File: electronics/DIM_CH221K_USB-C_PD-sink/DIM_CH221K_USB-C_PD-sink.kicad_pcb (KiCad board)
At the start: 2 copper layers, 17.3 x 18.5 mm, 15 parts, among them J1 USB-C_PD, J2 Conn_01x04, J3 Conn_01x04, U1 CH221K

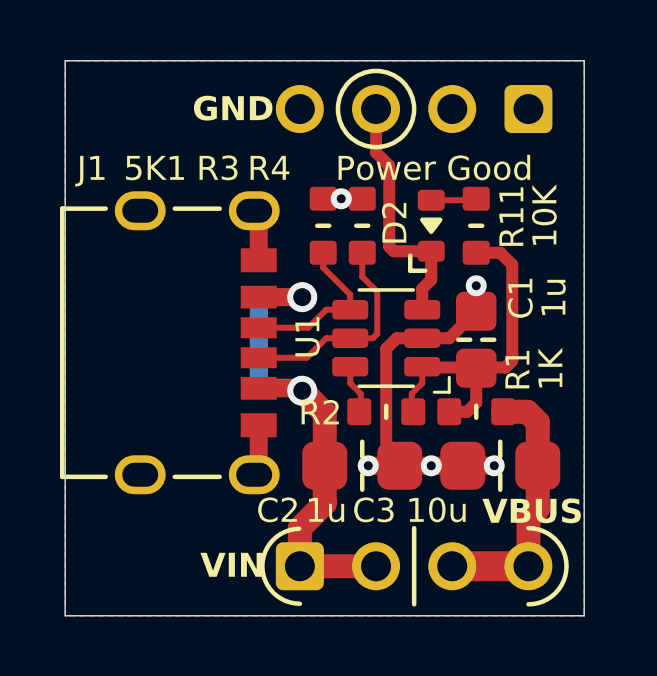
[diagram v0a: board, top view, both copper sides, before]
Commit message: small changes to CH221K with redundant components and adding labels
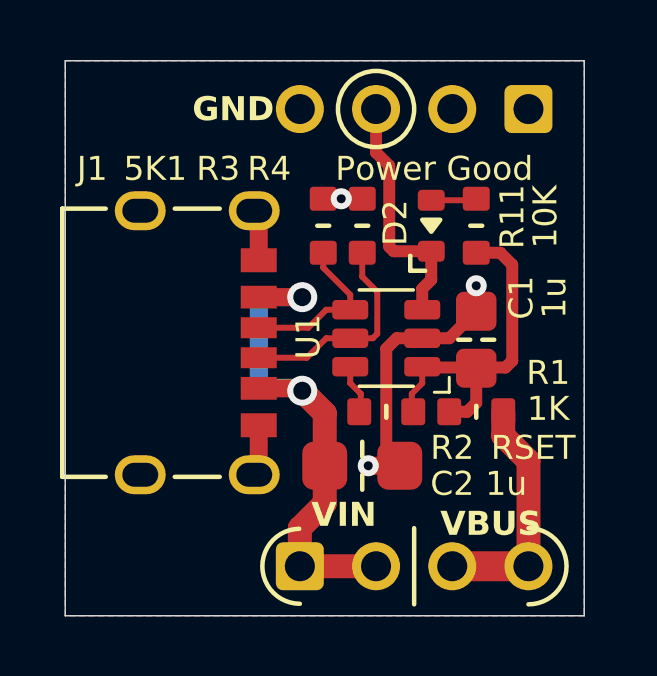
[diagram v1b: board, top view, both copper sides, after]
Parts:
- removed C3: 10u, SquantorCapacitor:C_1206_0805
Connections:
- net /VBUS renamed /VPOW
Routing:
- net GND: track 15.9 -> 12.7 mm, vias 5 -> 3
- net /VPOW: track 8.76 -> 8.04 mm

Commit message: changed label of CH221K power pin
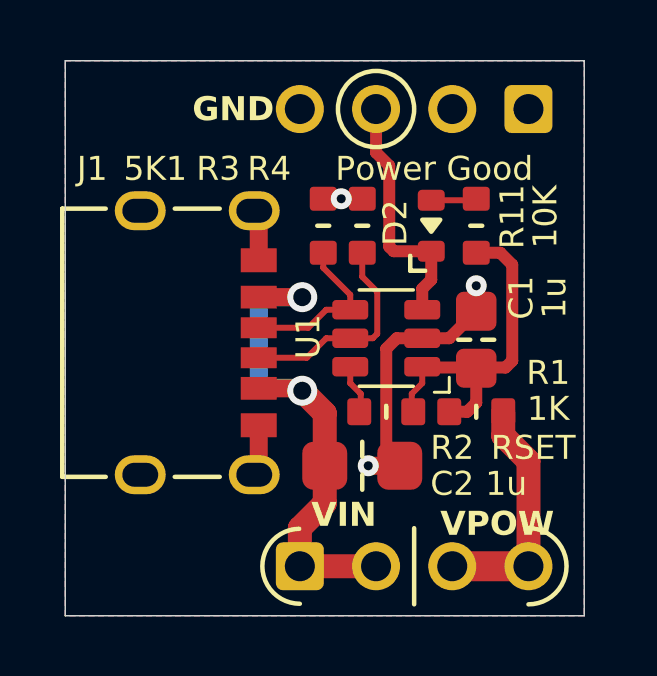
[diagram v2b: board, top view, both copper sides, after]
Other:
- board text added: "VPOW"
- board text removed: "VBUS"
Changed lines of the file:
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@@
 		(layer "Edge.Cuts")
 	)
-	(gr_text "VBUS"
+	(gr_text "VPOW"
 		(at 101.2 56.2 0)
 		(layer "F.SilkS")

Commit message: missed last changes, updated silk labels
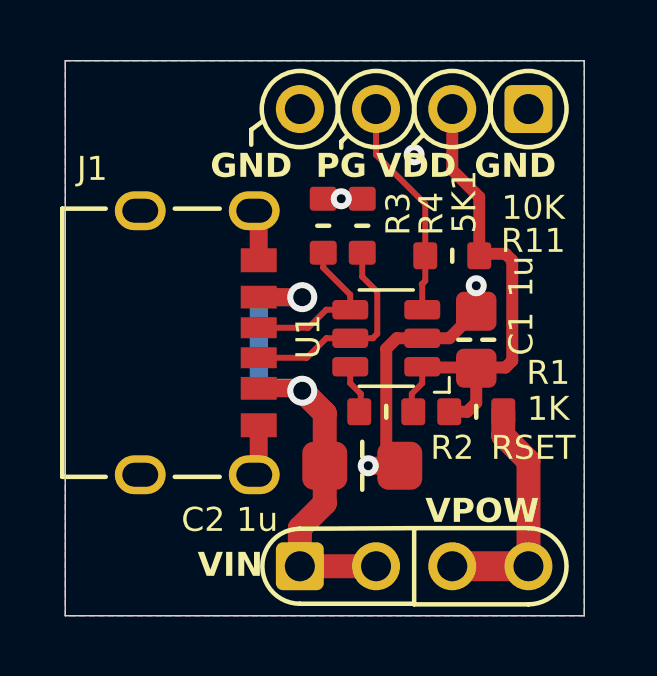
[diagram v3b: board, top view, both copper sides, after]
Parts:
- removed D2: Power Good, SquantorDiodes:LED_0603_hand
- moved R11 1.28 mm to (101.6, 46.8), turned to 180 degrees
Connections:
- J3 pad 2: GND -> /VDD
- R11 pad 2: Net-(D2-A) -> /PG
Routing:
- net /VDD: track 11.5 -> 16.8 mm
- net Net-(D2-A): track 1.52 -> 0.00 mm
- net /PG: track 8.31 -> 7.42 mm
- net GND: vias 3 -> 4
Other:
- board text added: "PG"
- board text added: "VDD"

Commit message: preparation for production V20260118
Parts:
- N1: value 20251001 -> 20260118
- moved N2 2.15 mm to (99.7, 49.4)
- moved N1 1.35 mm to (99.7, 53.0)
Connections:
- J2 pad 3: /VPOW -> GND
- J2 pad 4: /VPOW -> GND
- J3 pad 1: GND -> /VPOW
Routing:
- net /VPOW: track 8.04 -> 10.8 mm
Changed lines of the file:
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@@
 	(footprint "SquantorLabels:Label_Generic"
 		(layer "B.Cu")
-		(at 101 53.4 180)
+		(at 99.7 53.0375 180)
 		(descr "Label for general purpose use")
 		(tags "Label")
@@
 			)
 		)
-		(property "Value" "20251001"
+		(property "Value" "20260118"
 			(at 0 -0.0125 0)
 			(layer "B.SilkS")
@@
 	(footprint "Symbol:OSHW-Symbol_6.7x6mm_SilkScreen"
 		(layer "B.Cu")
-		(at 101.8 49.85 180)
+		(at 99.7 49.4 180)
 		(descr "Open Source Hardware Symbol")
 		(tags "Logo Symbol OSHW")
@@
 			(layers "*.Cu" "*.Mask")
 			(remove_unused_layers no)
-			(net 3 "/VPOW")
+			(net 1 "GND")
 			(pinfunction "Pin_3")
 			(pintype "passive")
@@
 			(layers "*.Cu" "*.Mask")
 			(remove_unused_layers no)
-			(net 3 "/VPOW")
+			(net 1 "GND")
 			(pinfunction "Pin_4")
 			(pintype "passive")
@@
 			(remove_unused_layers no)
 			(roundrect_rratio 0.15)
-			(net 1 "GND")
+			(net 3 "/VPOW")
 			(pinfunction "Pin_1")
 			(pintype "passive")
@@
 		)
 	)
-	(gr_text "VPOW"
+	(gr_text "GND"
 		(at 102.6 55.3 0)
 		(layer "F.SilkS")
@@
 		)
 	)
-	(gr_text "GND"
-		(at 103.7 43.8 0)
+	(gr_text "VPOW"
+		(at 104 43.8 0)
 		(layer "F.SilkS")
 		(effects
@@
 	)
 	(segment
-		(start 103.3 52.8)
-		(end 103.3 52)
-		(width 0.8)
+		(start 104.2 42.9)
+		(end 104.14 42.84)
+		(width 0.4)
 		(layer "F.Cu")
 		(net 3)
 	)
 	(segment
-		(start 104.14 53.64)
-		(end 103.3 52.8)
-		(width 0.8)
+		(start 104.14 42.84)
+		(end 104.14 41.91)
+		(width 0.4)
 		(layer "F.Cu")
 		(net 3)
 	)
 	(segment
-		(start 104.14 57.15)
-		(end 104.14 53.64)
-		(width 0.8)
+		(start 103.3 52)
+		(end 103.9 52)
+		(width 0.4)
 		(layer "F.Cu")
 		(net 3)
 	)
 	(segment
-		(start 101.6 57.15)
-		(end 104.14 57.15)
-		(width 1)
+		(start 104.2 51.7)
+		(end 104.2 42.9)
+		(width 0.4)
 		(layer "F.Cu")
 		(net 3)
+	)
+	(segment
+		(start 103.9 52)
+		(end 104.2 51.7)
+		(width 0.4)
+		(layer "F.Cu")
+		(net 3)
